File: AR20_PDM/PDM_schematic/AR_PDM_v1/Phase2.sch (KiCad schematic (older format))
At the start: 12 parts, among them Q2 BTS50025-1TAD, U9 INA233

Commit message: Alpha version DONE! - Gerber files generated
- Tweeked
- checked and re cheked
- added all missing components
- Created a really nice silkscreen
- Ready To Test
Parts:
- renumbered C_in4 to C27, C_out4 to C28, C_vs4 to C29, Cs4 to C30, C_bypass7 to C31, Q2 to Q6, R10 to R25, R_in4 to R26, R_sense4 to R27, R_s4 to R28, R_Shunt8 to R29, U9 to U6

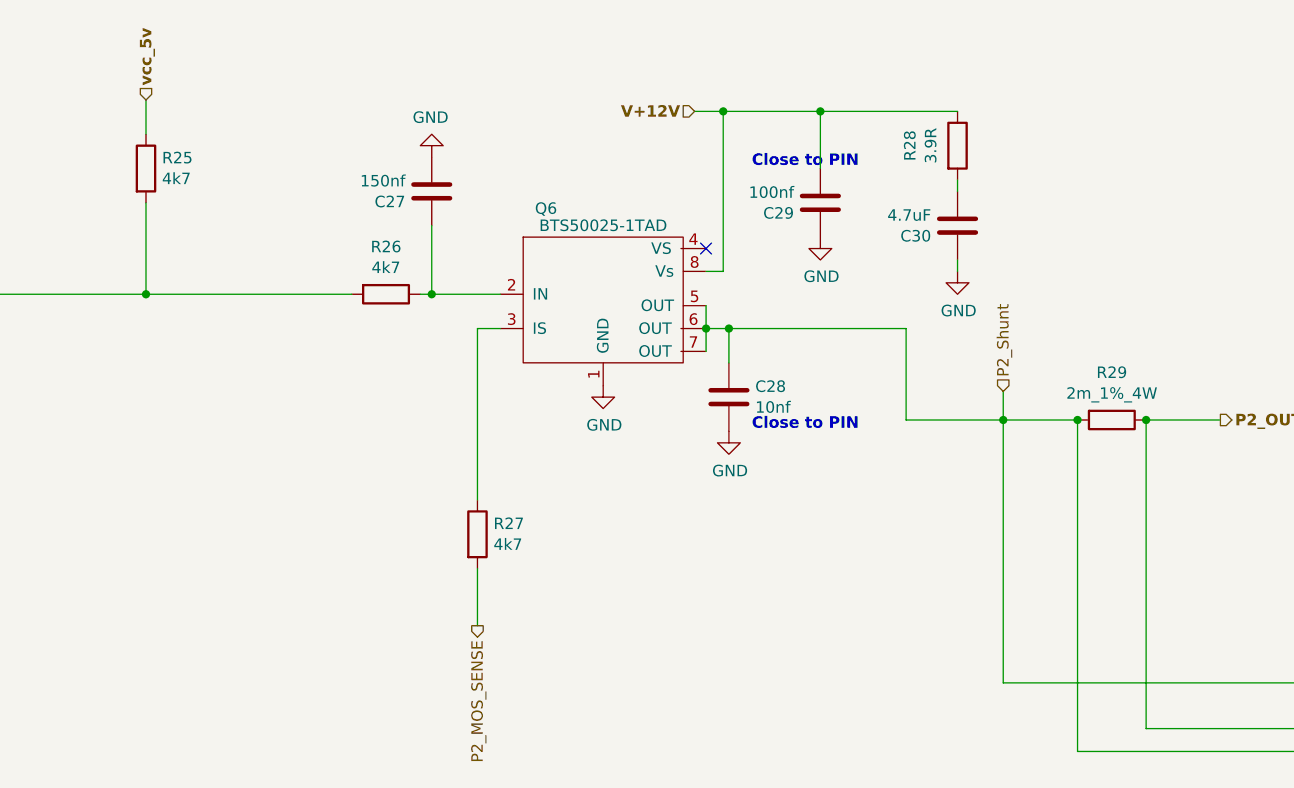
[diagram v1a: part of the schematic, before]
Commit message: Fixed wrong resistors, mos sense. Gerber files updated
- removed all R_is_protection resistors on each mosfet line
- added one R_is_protection resistors to mos_sense_all
ps, mux N-fets, does not need overvoltage protection. 60 volt tolerant.
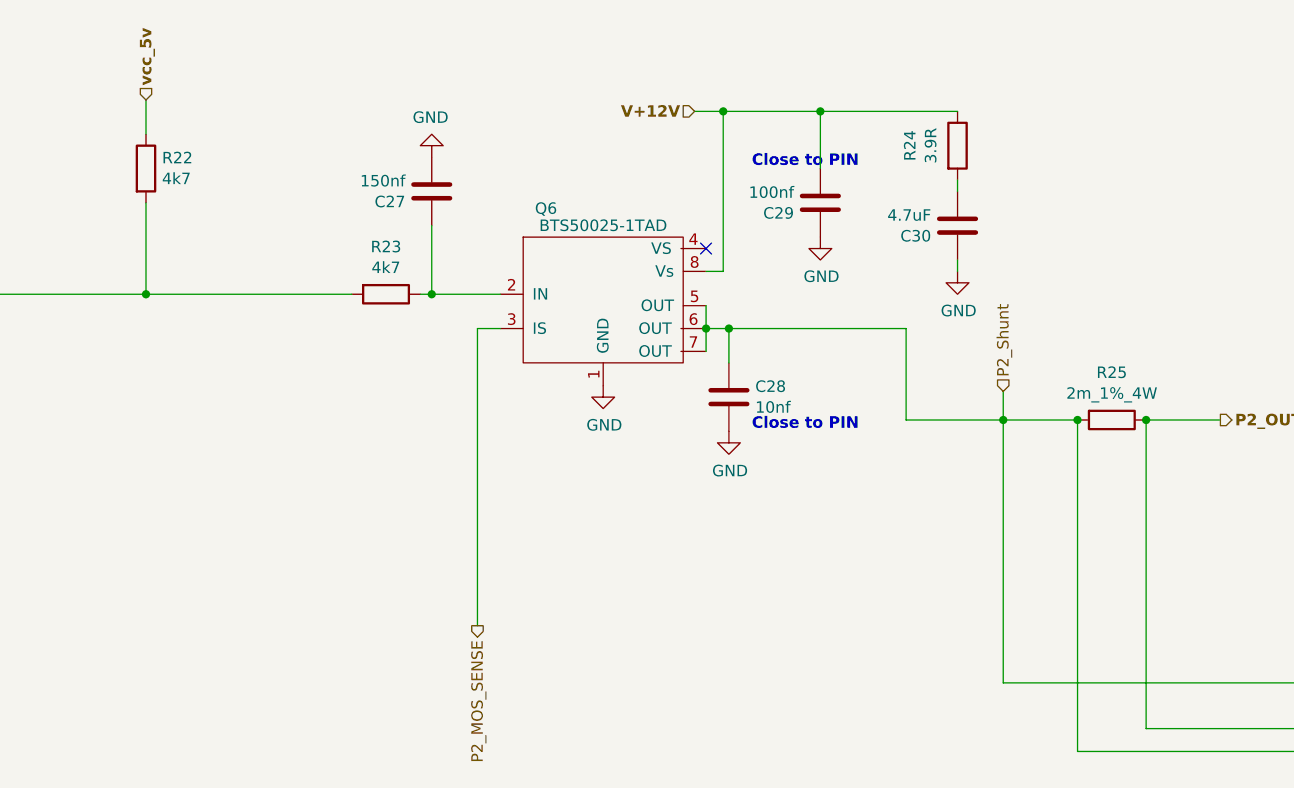
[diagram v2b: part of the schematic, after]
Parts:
- removed R27: 4k7, Resistor_SMD:R_0603_1608Metric, symbol AR20_PDM_v1-rescue:R-Device
- renumbered R25 to R22, R26 to R23, R28 to R24, R29 to R25
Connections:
- net P2_MOS_SENSE: now also Q6.3 (IS)
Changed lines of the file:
@@
 AR Path="/5E0E594B/5E21B808" Ref="R?"  Part="1"
 AR Path="/5E0E607C/5E21B808" Ref="R?"  Part="1"
-AR Path="/5E0FB5C8/5E21B808" Ref="R26"  Part="1"
+AR Path="/5E0FB5C8/5E21B808" Ref="R23"  Part="1"
 AR Path="/5E0FBBBD/5E21B808" Ref="R?"  Part="1"
 AR Path="/5E0FC3A2/5E21B808" Ref="R?"  Part="1"
@@
 AR Path="/5E0FDCCC/5E21B808" Ref="R?"  Part="1"
 AR Path="/5E10174B/5E21B808" Ref="R?"  Part="1"
-F 0 "R26" V 3093 2400 50  0000 C CNN
+F 0 "R23" V 3093 2400 50  0000 C CNN
 F 1 "4k7" V 3184 2400 50  0000 C CNN
 F 2 "Resistor_SMD:R_0603_1608Metric" V 3230 2400 50  0001 C CNN
@@
 AR Path="/5E0E594B/5E21B819" Ref="R?"  Part="1"
 AR Path="/5E0E607C/5E21B819" Ref="R?"  Part="1"
-AR Path="/5E0FB5C8/5E21B819" Ref="R25"  Part="1"
+AR Path="/5E0FB5C8/5E21B819" Ref="R22"  Part="1"
 AR Path="/5E0FBBBD/5E21B819" Ref="R?"  Part="1"
 AR Path="/5E0FC3A2/5E21B819" Ref="R?"  Part="1"
@@
 AR Path="/5E0FDCCC/5E21B819" Ref="R?"  Part="1"
 AR Path="/5E10174B/5E21B819" Ref="R?"  Part="1"
-F 0 "R25" H 2320 1896 50  0000 L CNN
+F 0 "R22" H 2320 1896 50  0000 L CNN
 F 1 "4k7" H 2320 1805 50  0000 L CNN
 F 2 "Resistor_SMD:R_0603_1608Metric" V 2180 1850 50  0001 C CNN
@@
 	3700 2550 3800 2550
 Wire Wire Line
-	3700 3850 3700 3600
-Wire Wire Line
 	8750 2850 8750 3350
 Wire Wire Line
@@
 AR Path="/5E0E594B/5E21B86C" Ref="R?"  Part="1"
 AR Path="/5E0E607C/5E21B86C" Ref="R?"  Part="1"
-AR Path="/5E0FB5C8/5E21B86C" Ref="R28"  Part="1"
+AR Path="/5E0FB5C8/5E21B86C" Ref="R24"  Part="1"
 AR Path="/5E0FBBBD/5E21B86C" Ref="R?"  Part="1"
 AR Path="/5E0FC3A2/5E21B86C" Ref="R?"  Part="1"
@@
 AR Path="/5E0FDCCC/5E21B86C" Ref="R?"  Part="1"
 AR Path="/5E10174B/5E21B86C" Ref="R?"  Part="1"
-F 0 "R28" V 5593 1750 50  0000 C CNN
+F 0 "R24" V 5593 1750 50  0000 C CNN
 F 1 "3.9R" V 5684 1750 50  0000 C CNN
 F 2 "Resistor_SMD:R_0603_1608Metric" V 5730 1750 50  0001 C CNN
@@
 Wire Wire Line
 	6000 4100 8750 4100
-$Comp
-L AR20_PDM_v1-rescue:R-Device R?
-U 1 1 5E21B872
-P 3700 3450
-AR Path="/5DA89415/5E21B872" Ref="R?"  Part="1"
-AR Path="/5DEB10A1/5E21B872" Ref="R?"  Part="1"
-AR Path="/5DEB20EA/5E21B872" Ref="R?"  Part="1"
-AR Path="/5E0E4725/5E21B872" Ref="R?"  Part="1"
-AR Path="/5E0E4A93/5E21B872" Ref="R?"  Part="1"
-AR Path="/5E0E4EB5/5E21B872" Ref="R?"  Part="1"
-AR Path="/5E0E5304/5E21B872" Ref="R?"  Part="1"
-AR Path="/5E0E594B/5E21B872" Ref="R?"  Part="1"
-AR Path="/5E0E607C/5E21B872" Ref="R?"  Part="1"
-AR Path="/5E0FB5C8/5E21B872" Ref="R27"  Part="1"
-AR Path="/5E0FBBBD/5E21B872" Ref="R?"  Part="1"
-AR Path="/5E0FC3A2/5E21B872" Ref="R?"  Part="1"
-AR Path="/5E0FCFDC/5E21B872" Ref="R?"  Part="1"
-AR Path="/5E0FDCCC/5E21B872" Ref="R?"  Part="1"
-AR Path="/5E10174B/5E21B872" Ref="R?"  Part="1"
-F 0 "R27" H 3770 3496 50  0000 L CNN
-F 1 "4k7" H 3770 3405 50  0000 L CNN
-F 2 "Resistor_SMD:R_0603_1608Metric" V 3630 3450 50  0001 C CNN
-F 3 "~" H 3700 3450 50  0001 C CNN
-	1    3700 3450
-	1    0    0    -1
-$EndComp
 Wire Wire Line
 	6325 4400 8750 4400
@@
 AR Path="/5E0E594B/5E1B69BA" Ref="R?"  Part="1"
 AR Path="/5E0E607C/5E1B69BA" Ref="R?"  Part="1"
-AR Path="/5E0FB5C8/5E1B69BA" Ref="R29"  Part="1"
+AR Path="/5E0FB5C8/5E1B69BA" Ref="R25"  Part="1"
 AR Path="/5E0FBBBD/5E1B69BA" Ref="R?"  Part="1"
 AR Path="/5E0FC3A2/5E1B69BA" Ref="R?"  Part="1"
@@
 AR Path="/5E0FDCCC/5E1B69BA" Ref="R?"  Part="1"
 AR Path="/5E10174B/5E1B69BA" Ref="R?"  Part="1"
-F 0 "R29" V 6268 2950 50  0000 C CNN
+F 0 "R25" V 6268 2950 50  0000 C CNN
 F 1 "2m_1%_4W" V 6359 2950 50  0000 C CNN
 F 2 "Resistor_SMD:R_2512_6332Metric" V 6405 2950 50  0001 C CNN
@@
 Text HLabel 6000 2825 1    50   Input ~ 0
 P2_Shunt
-Wire Wire Line
-	3700 2550 3700 3300
 Wire Wire Line
 	4650 1600 4775 1600
@@
 Wire Wire Line
 	4775 1600 5200 1600
+Wire Wire Line
+	3700 2550 3700 3850
 $EndSCHEMATC

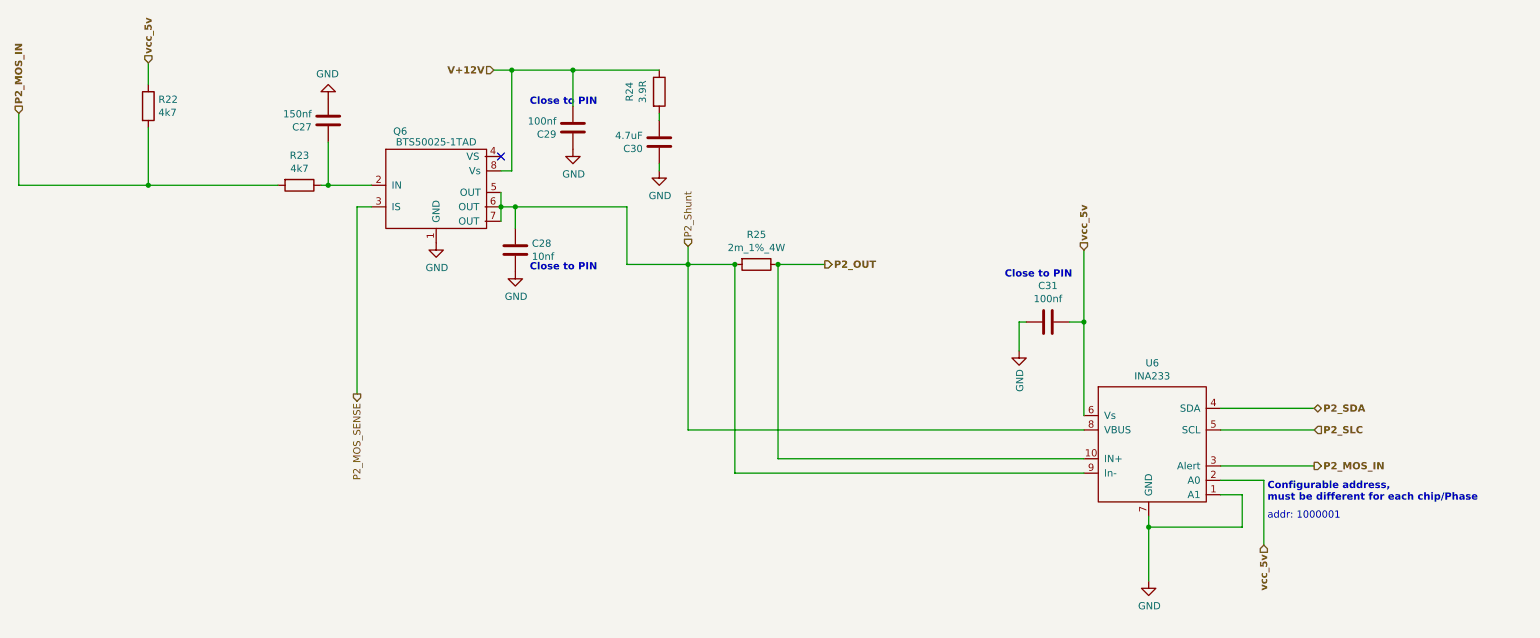
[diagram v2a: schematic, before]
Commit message: Major redesign. schematics completed, PCB work in progress
-TODO : A proper changelog file. Where all changes will apear 
- Redesigned schematics to accommodate errors in the improvement list
- More detail in ALPHA improvement list
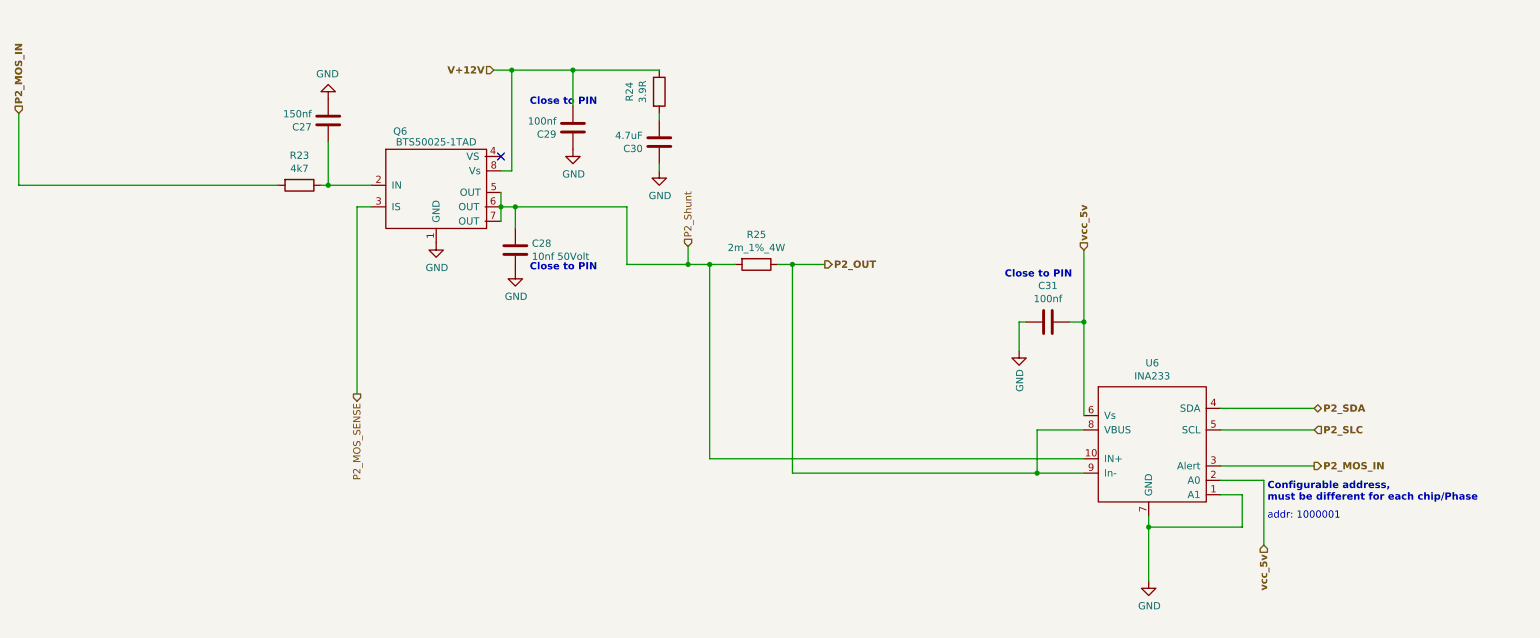
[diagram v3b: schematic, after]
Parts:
- removed R22: 4k7, Resistor_SMD:R_0603_1608Metric, symbol AR20_PDM_v1-rescue:R-Device
- C28: value 10nf -> 10nf 50Volt
- R24: footprint Resistor_SMD:R_0603_1608Metric -> Resistor_SMD:R_2512_6332Metric
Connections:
- net P2_OUT: now also U6.8 (VBUS), U6.9 (In-); no longer U6.10 (IN+)
- net P2_Shunt: now also U6.10 (IN+); no longer U6.8 (VBUS), U6.9 (In-)
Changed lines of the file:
@@
 $Descr A4 11693 8268
 encoding utf-8
-Sheet 6 13
+Sheet 6 14
 Title ""
 Date ""
@@
 AR Path="/5E10174B/5E21B80E" Ref="C?"  Part="1"
 F 0 "C28" H 4915 2896 50  0000 L CNN
-F 1 "10nf" H 4915 2805 50  0000 L CNN
+F 1 "10nf 50Volt" H 4915 2805 50  0000 L CNN
 F 2 "Capacitor_SMD:C_0603_1608Metric" H 4838 2700 50  0001 C CNN
 F 3 "~" H 4800 2850 50  0001 C CNN
@@
 $EndComp
 $Comp
-L AR20_PDM_v1-rescue:R-Device R?
-U 1 1 5E21B819
-P 2250 1850
-AR Path="/5DA89415/5E21B819" Ref="R?"  Part="1"
-AR Path="/5DEB10A1/5E21B819" Ref="R?"  Part="1"
-AR Path="/5DEB20EA/5E21B819" Ref="R?"  Part="1"
-AR Path="/5E0E4725/5E21B819" Ref="R?"  Part="1"
-AR Path="/5E0E4A93/5E21B819" Ref="R?"  Part="1"
-AR Path="/5E0E4EB5/5E21B819" Ref="R?"  Part="1"
-AR Path="/5E0E5304/5E21B819" Ref="R?"  Part="1"
-AR Path="/5E0E594B/5E21B819" Ref="R?"  Part="1"
-AR Path="/5E0E607C/5E21B819" Ref="R?"  Part="1"
-AR Path="/5E0FB5C8/5E21B819" Ref="R22"  Part="1"
-AR Path="/5E0FBBBD/5E21B819" Ref="R?"  Part="1"
-AR Path="/5E0FC3A2/5E21B819" Ref="R?"  Part="1"
-AR Path="/5E0FCFDC/5E21B819" Ref="R?"  Part="1"
-AR Path="/5E0FDCCC/5E21B819" Ref="R?"  Part="1"
-AR Path="/5E10174B/5E21B819" Ref="R?"  Part="1"
-F 0 "R22" H 2320 1896 50  0000 L CNN
-F 1 "4k7" H 2320 1805 50  0000 L CNN
-F 2 "Resistor_SMD:R_0603_1608Metric" V 2180 1850 50  0001 C CNN
-F 3 "~" H 2250 1850 50  0001 C CNN
-	1    2250 1850
-	1    0    0    -1
-$EndComp
-$Comp
 L AR20_PDM_v1-rescue:C-Device C?
 U 1 1 5DAAC201
@@
 Text Notes 8200 3050 0    50   ~ 10
 Close to PIN
-Text HLabel 2250 1550 1    50   Input ~ 10
-vcc_5v
 Wire Wire Line
 	9700 4100 10350 4100
-Wire Wire Line
-	2250 1550 2250 1700
 $Comp
 L AR20_PDM_v1-rescue:C-Device C?
@@
 F 0 "R24" V 5593 1750 50  0000 C CNN
 F 1 "3.9R" V 5684 1750 50  0000 C CNN
-F 2 "Resistor_SMD:R_0603_1608Metric" V 5730 1750 50  0001 C CNN
+F 2 "Resistor_SMD:R_2512_6332Metric" V 5730 1750 50  0001 C CNN
 F 3 "~" H 5800 1750 50  0001 C CNN
 	1    5800 1750
@@
 Wire Wire Line
 	9700 4350 10350 4350
-Connection ~ 2250 2400
-Wire Wire Line
-	2250 2000 2250 2400
 Wire Wire Line
 	1350 1900 1350 2400
-Wire Wire Line
-	1350 2400 2250 2400
 Text Notes 10025 4600 0    50   ~ 10
 Configurable address, \nmust be different for each chip/Phase
@@
 	5575 2550 5575 2950
 Connection ~ 4800 2550
-Wire Wire Line
-	6000 4100 8750 4100
-Wire Wire Line
-	6325 4400 8750 4400
 Text HLabel 3700 3850 3    50   Output ~ 0
 P2_MOS_SENSE
-Wire Wire Line
-	6625 2950 6625 4300
-Wire Wire Line
-	6325 2950 6325 4400
 Connection ~ 6000 2950
 Wire Wire Line
-	6000 2950 6325 2950
-Wire Wire Line
-	6000 4100 6000 2950
+	6000 2950 6150 2950
 Wire Wire Line
 	5575 2950 6000 2950
@@
 Text HLabel 4650 1600 0    50   Input ~ 10
 V+12V
-Wire Wire Line
-	2250 2400 3150 2400
 $Comp
 L AR20_PDM_v1-rescue:R-Device R?
@@
 $EndComp
 Wire Wire Line
-	6625 2950 6950 2950
-Connection ~ 6325 2950
-Connection ~ 6625 2950
-Wire Wire Line
-	6625 4300 8750 4300
+	6625 2950 6725 2950
 Text Notes 10025 4725 0    50   ~ 0
 addr: 1000001
@@
 Wire Wire Line
 	3700 2550 3700 3850
+Wire Wire Line
+	1350 2400 3150 2400
+Wire Wire Line
+	8750 4300 6150 4300
+Wire Wire Line
+	6150 4300 6150 2950
+Wire Wire Line
+	8750 4400 8425 4400
+Wire Wire Line
+	6725 4400 6725 2950
+Wire Wire Line
+	8750 4100 8425 4100
+Wire Wire Line
+	8425 4100 8425 4400
+Connection ~ 8425 4400
+Wire Wire Line
+	8425 4400 6725 4400
+Connection ~ 6725 2950
+Wire Wire Line
+	6725 2950 6950 2950
+Connection ~ 6150 2950
+Wire Wire Line
+	6150 2950 6325 2950
 $EndSCHEMATC

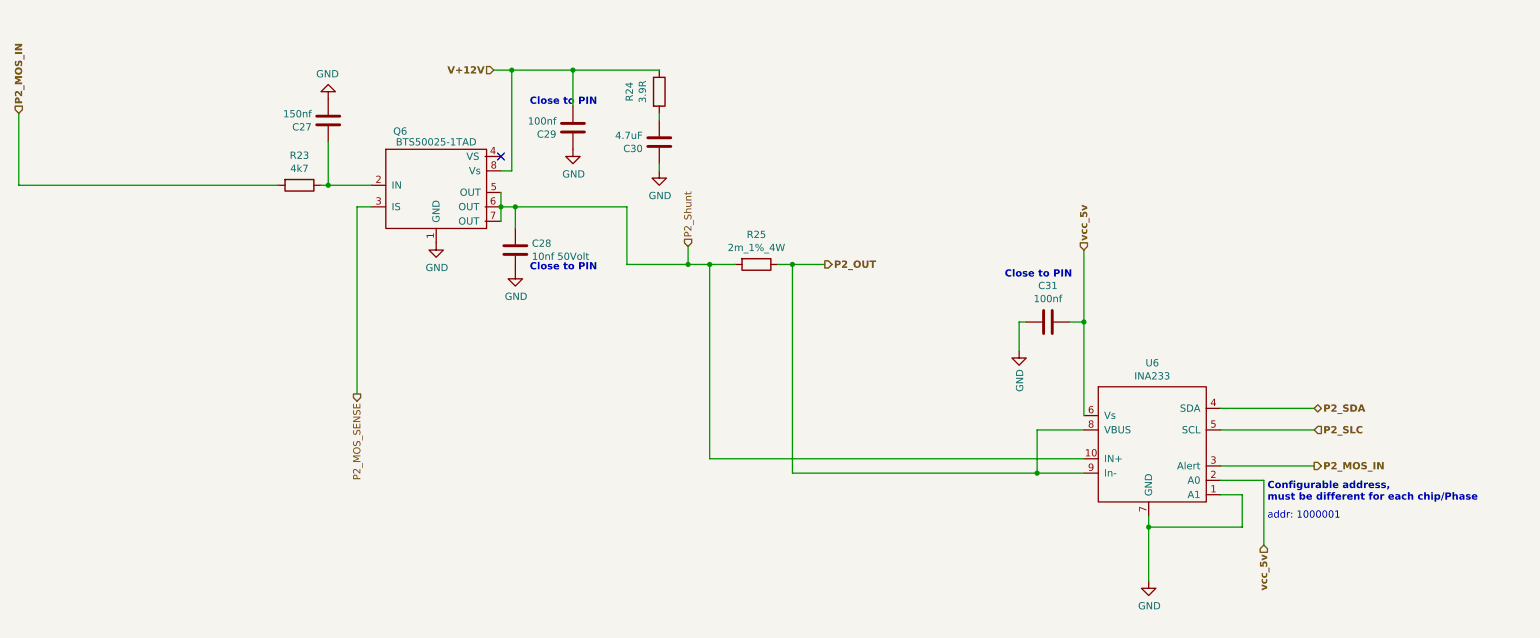
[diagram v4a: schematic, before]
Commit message: schematics rework
Fixed INA233 frying due to inductive flyback:
- Paced ina233 high side of the mosftets
- New input protection reseistors, and zener diodes, on each ina233.
Simplified:
- Removed the MUX and mos sense lines, as i realize that most of this functionality can be obtained trough INA233.
- Removed some of the cappacitors , besides the most needed ones.
- removed  back to back zener diode configuration, now a single diode insted.
 to reduce negative voltage in case of loss of VS, to be easy on the INA233 filters.
new stuff:
- Another temp sensor.
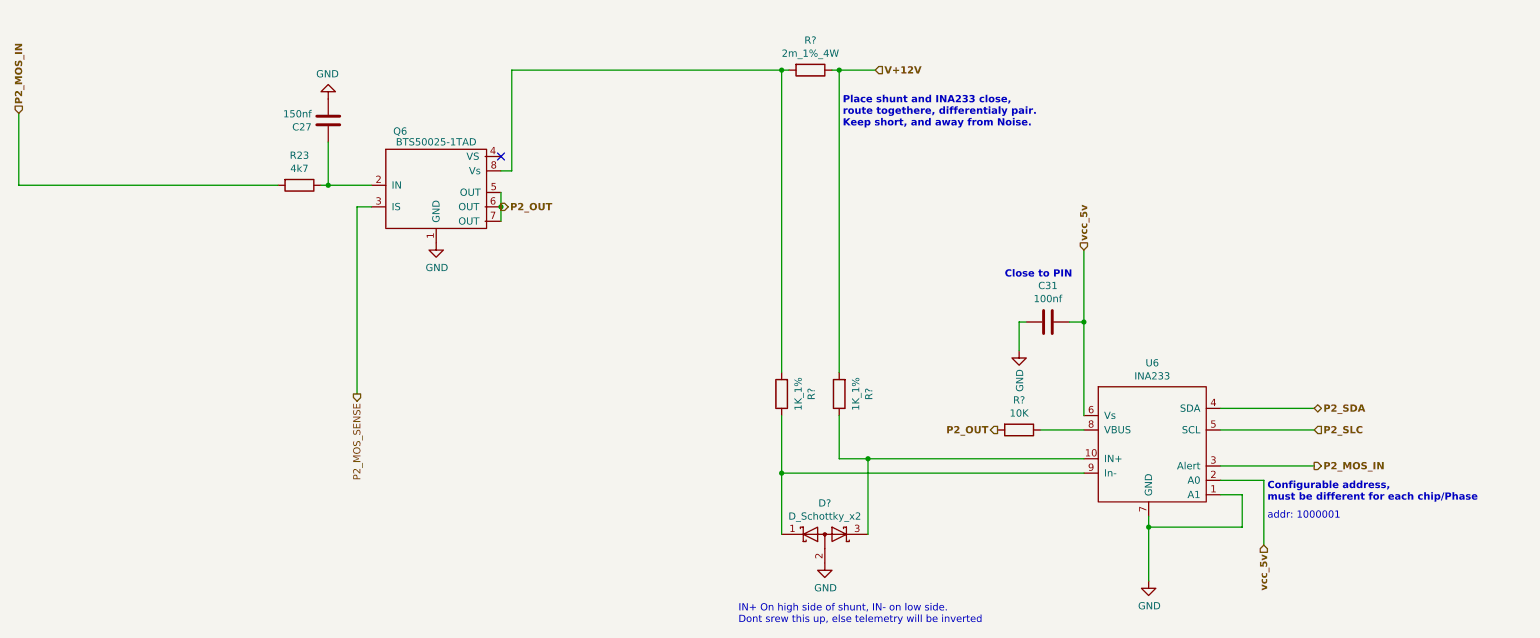
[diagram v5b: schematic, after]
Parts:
- removed C28: 10nf 50Volt, Capacitor_SMD:C_0603_1608Metric, symbol AR20_PDM_v1-rescue:C-Device
- removed C29: 100nf, Capacitor_SMD:C_0603_1608Metric, symbol AR20_PDM_v1-rescue:C-Device
- removed C30: 4.7uF, Capacitor_SMD:C_1206_3216Metric, symbol AR20_PDM_v1-rescue:C-Device
- removed R24: 3.9R, Resistor_SMD:R_2512_6332Metric, symbol AR20_PDM_v1-rescue:R-Device
- removed R25: 2m_1%_4W, Resistor_SMD:R_2512_6332Metric, symbol AR20_PDM_v1-rescue:R-Device
- added D?: D_Schottky_x2, symbol AR20_PDM_v1-rescue:D_Schottky_x2
- added R?: 2m_1%_4W, Resistor_SMD:R_2512_6332Metric, symbol AR20_PDM_v1-rescue:R-Device
- added R? (x2): 1K_1%, Resistor_SMD:R_0603_1608Metric, symbol AR20_PDM_v1-rescue:R-Device
- added R?: 10K, Resistor_SMD:R_0603_1608Metric, symbol AR20_PDM_v1-rescue:R-Device
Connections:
- net GND: now also D?.2 (A)
- net P2_OUT: now also Q6.5 (OUT), Q6.6 (OUT), Q6.7 (OUT), R?.2; no longer U6.8 (VBUS), U6.9 (In-)
- net V+12V: now also R?.1, R?.2; no longer Q6.8 (Vs)
- removed net P2_Shunt: Q6.5 (OUT), Q6.6 (OUT), Q6.7 (OUT), U6.10 (IN+)
- new net: Q6.8 (Vs), R?.2, R?.2
- new net: D?.3 (K), R?.1, U6.10 (IN+)
- new net: R?.1, U6.8 (VBUS)
- new net: D?.1 (K), R?.1, U6.9 (In-)
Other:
- note added: "IN+ On high side of shunt, IN- on low side.\nDont srew this up, else telemetry will be inverted"
- note added: "Place shunt and INA233 close, \nroute togethere, differentialy pair. \nKeep short, and away from Noise."
